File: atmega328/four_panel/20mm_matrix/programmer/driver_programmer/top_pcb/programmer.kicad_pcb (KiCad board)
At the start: 2 copper layers, 50 x 140 mm, 25 parts, among them P1 CONN_3X2, P10 CONN_2, P11 CONN_6, P12 CONN_2, P13 CONN_6, P2 CONN_3X2, P3 CONN_3X2, P4 CONN_3X2, P5 CONN_3X2, P6 CONN_2, P7 CONN_6, P8 CONN_2, P9 CONN_6

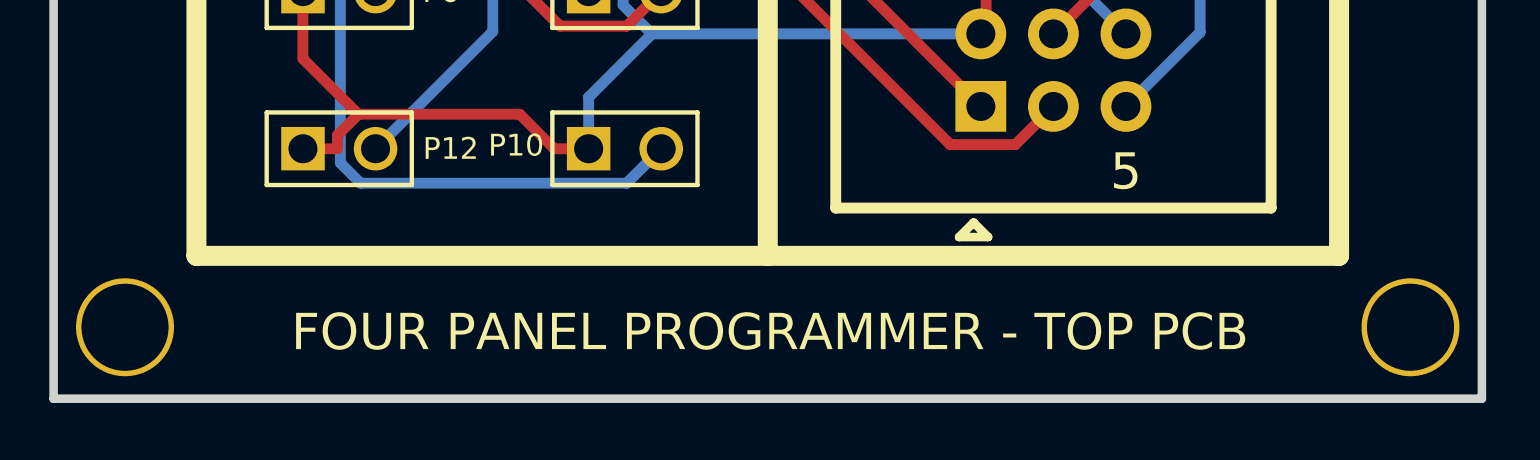
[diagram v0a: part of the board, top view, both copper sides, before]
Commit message: Added bottom pcb for 4x20mm atmega328 panel driver.
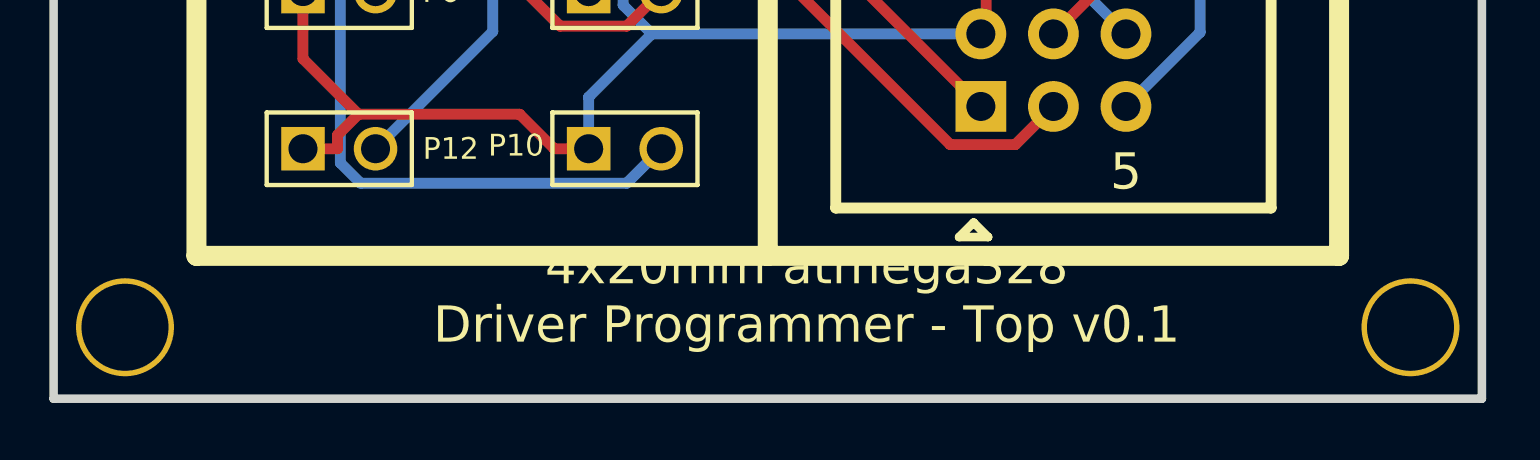
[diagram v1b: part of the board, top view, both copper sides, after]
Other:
- board text added: "4x20mm atmega328 Driver Programmer - Top v0.1"
- board text removed: "FOUR PANEL PROGRAMMER - TOP PCB"
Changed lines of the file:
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@@
     (links 116)
     (no_connects 0)
-    (area 0 0 0 0)
+    (area 43.837667 44.131 96.162333 186.631)
     (thickness 1.6)
     (drawings 27)
@@
     (effects (font (size 1.27 1.27) (thickness 0.254)))
   )
-  (gr_text "FOUR PANEL PROGRAMMER - TOP PCB" (at 70.0786 182.6768) (layer F.SilkS)
+  (gr_text "4x20mm atmega328 \nDriver Programmer - Top v0.1" (at 71.3613 181.3941) (layer F.SilkS)
     (effects (font (size 1.27 1.27) (thickness 0.254)))
   )

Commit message: Added annotations to 4x20mm atmega328 driver programmer top pcb.
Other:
- board text added: "BOTTOM"
- board text added: "TOP"
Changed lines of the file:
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@@
     (area 43.837667 44.131 96.162333 186.631)
     (thickness 1.6)
-    (drawings 27)
+    (drawings 33)
     (tracks 664)
     (zones 0)
@@
     )
   )
+  (gr_text BOTTOM (at 60 132.5) (layer B.SilkS)
+    (effects (font (size 1.5 1.5) (thickness 0.3)) (justify mirror))
+  )
+  (gr_text TOP (at 59.5 97) (layer B.SilkS)
+    (effects (font (size 1.5 1.5) (thickness 0.3)) (justify mirror))
+  )
+  (gr_line (start 90 135) (end 90 95) (angle 90) (layer B.SilkS) (width 0.7))
+  (gr_line (start 50 135) (end 90 135) (angle 90) (layer B.SilkS) (width 0.7))
+  (gr_line (start 50 95) (end 50 135) (angle 90) (layer B.SilkS) (width 0.7))
+  (gr_line (start 90 95) (end 50 95) (angle 90) (layer B.SilkS) (width 0.7))
   (gr_text www.iorodeo.com (at 69.8754 47.117) (layer F.SilkS)
     (effects (font (size 1.27 1.27) (thickness 0.254)))
